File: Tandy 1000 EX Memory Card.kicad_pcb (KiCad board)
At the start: 2 copper layers, 57.2 x 84.5 mm, 17 parts, among them J1 Tandy_Expansion, J2 Tandy_Expansion, U1 AS6C4008-55PCN, U2 74LS00, U4 74LS32, U5 74LS245

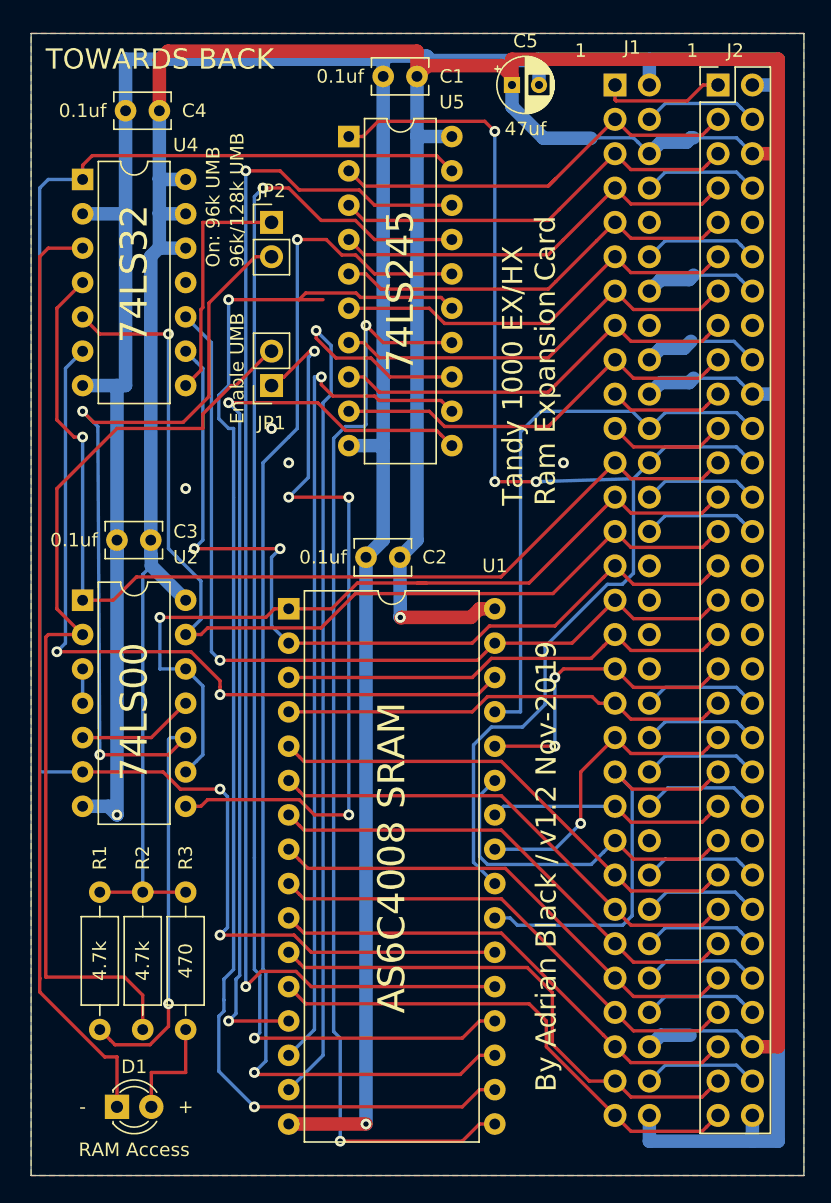
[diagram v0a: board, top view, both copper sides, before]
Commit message: Updated with OSHW Logo/License
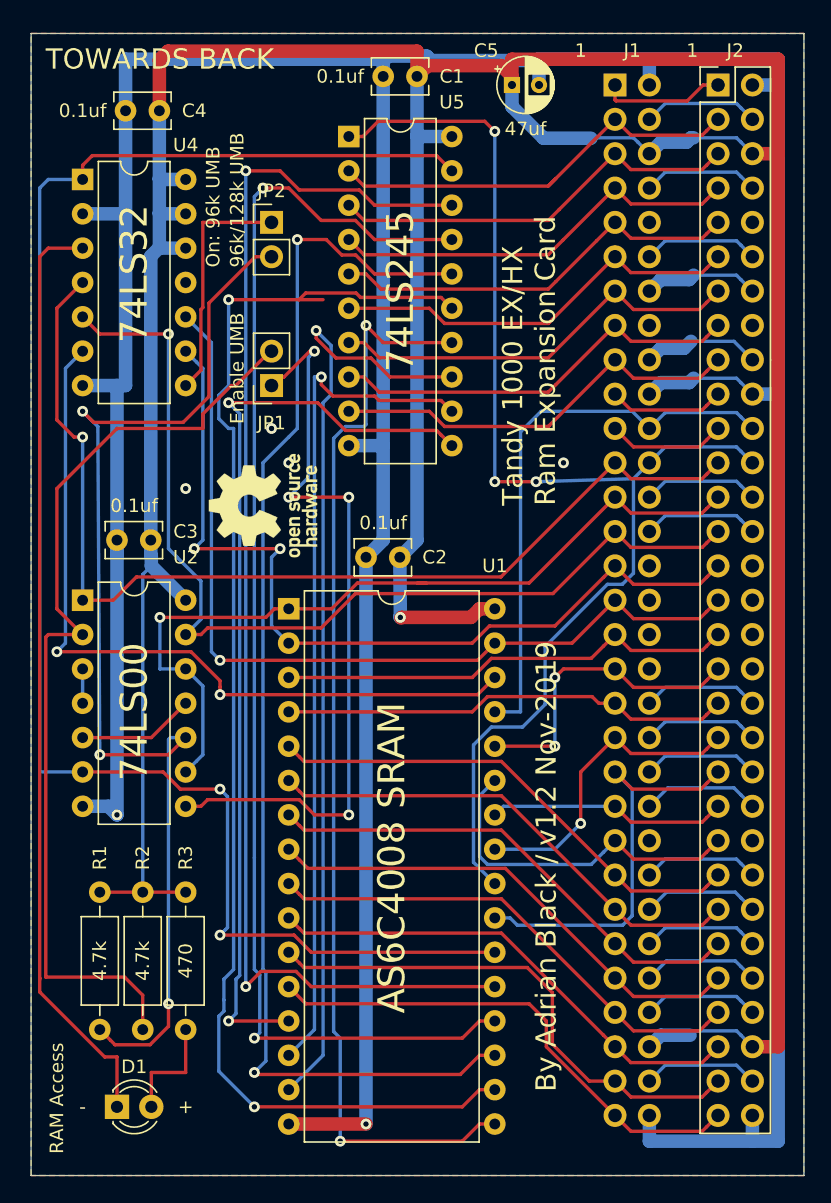
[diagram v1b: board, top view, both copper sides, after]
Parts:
- added REF**: OSHW, Symbol:OSHW-Logo_7.5x8mm_SilkScreen, F.Cu at (132.7, 87.6)
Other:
- board text added: "Adrian's Digital Basement"
- board text added: "https://www.youtube.com/user/craig1black"
